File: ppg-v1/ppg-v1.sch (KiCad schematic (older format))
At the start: 67 parts

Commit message: Added everything together, moved things around, added a battery, and made some changes to the circuitry controlling charging etc
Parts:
- removed C?: 1uF, symbol Device:C_Small
- removed D? (x2): IN-S85TATRGB_ALT, rcpaperplane:IN-S85TATRGB, symbol rcpaperplane:IN-S85TATRGB_ALT
- removed R?: 100K, Resistor_SMD:R_0603_1608Metric, symbol Device:R
- removed R?: 1K, Resistor_SMD:R_0603_1608Metric, symbol Device:R
- removed U? (x2): SN74LVC1GU04, Package_TO_SOT_SMD:SOT-353_SC-70-5, symbol rcpaperplane:SN74LVC1GU04
- added BT?: Battery, symbol Device:Battery
- gave numbers to parts that had none: 1
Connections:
- net labels added: VBAT
- wire segments 127 -> 117
- no-connect marks 21 -> 20
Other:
- moved on the sheet: C?, D?, D?A, R?, SW?, U?, U?A, U?B, U?C, UC, Y?

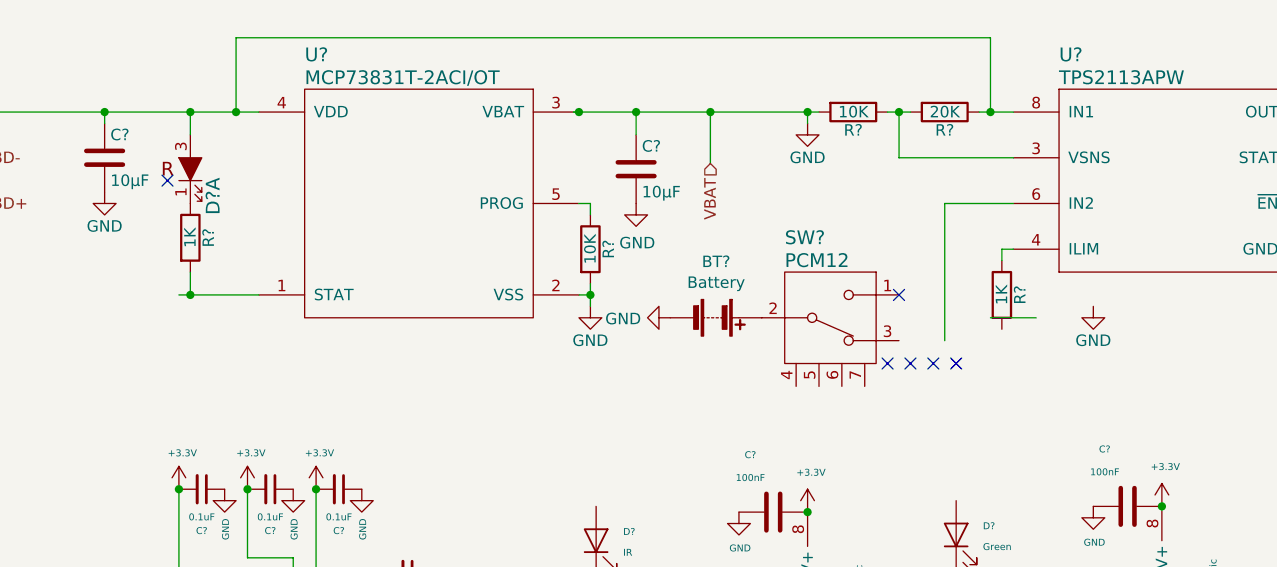
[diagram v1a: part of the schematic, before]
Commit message: Fixed some offset parts and a disconnect between a part and GND
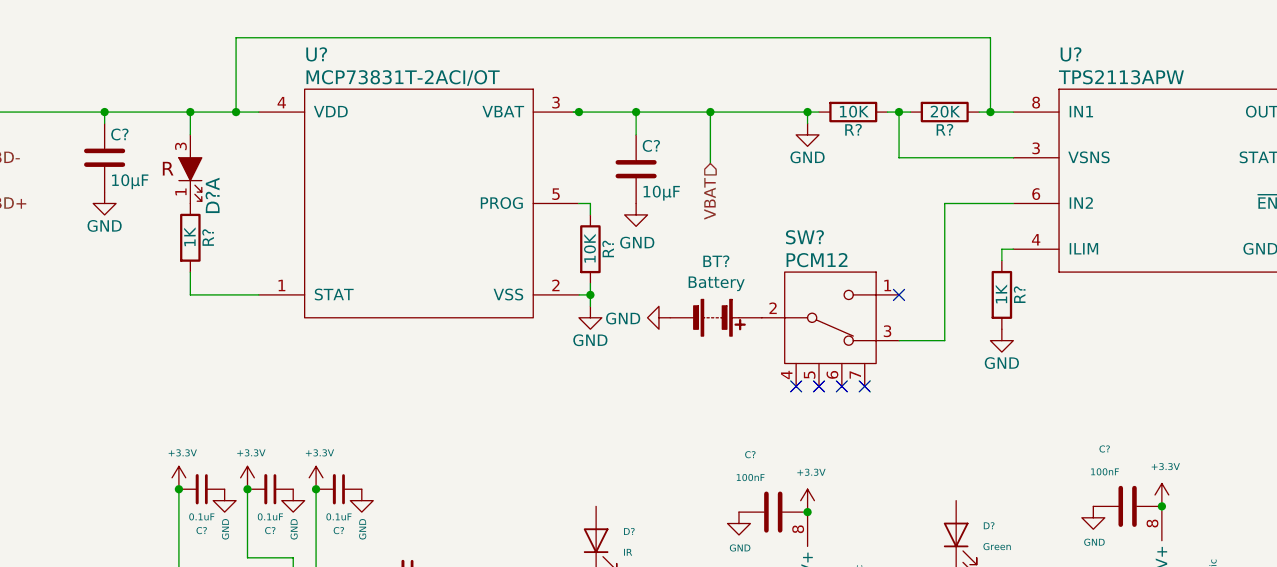
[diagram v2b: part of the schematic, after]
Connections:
- wire segments 117 -> 116
- no-connect marks 20 -> 19
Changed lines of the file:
@@
 Wire Wire Line
 	2375 925  2375 975
-NoConn ~ 2650 1225
 $Comp
 L Device:R R?
@@
 $EndComp
 Wire Wire Line
-	2700 1725 2750 1725
-Wire Wire Line
 	2750 1725 2750 1625
 Wire Wire Line
@@
 L power:GND #PWR0127
 U 1 1 5B12E1D7
-P 6700 1775
-F 0 "#PWR0127" H 6700 1525 50  0001 C CNN
-F 1 "GND" H 6700 1625 50  0000 C CNN
-F 2 "" H 6700 1775 50  0001 C CNN
-F 3 "" H 6700 1775 50  0001 C CNN
-	1    6700 1775
+P 6300 1875
+F 0 "#PWR0127" H 6300 1625 50  0001 C CNN
+F 1 "GND" H 6300 1725 50  0000 C CNN
+F 2 "" H 6300 1875 50  0001 C CNN
+F 3 "" H 6300 1875 50  0001 C CNN
+	1    6300 1875
 	1    0    0    -1
 $EndComp
@@
 	6050 1325 6050 1925
 NoConn ~ 5850 1725
-NoConn ~ 5800 2025
-NoConn ~ 5900 2025
-NoConn ~ 6000 2025
-NoConn ~ 6100 2025
+NoConn ~ 5500 2125
+NoConn ~ 5600 2125
+NoConn ~ 5700 2125
 $Comp
 L Device:C C?
@@
 RX_IND
 Wire Wire Line
-	6450 1825 6250 1825
-Wire Wire Line
 	5850 925  5900 925
 Wire Wire Line
@@
 	0    1    1    0
 $EndComp
-Connection ~ 2750 1725
 Wire Wire Line
 	2750 925  2375 925
 Connection ~ 2750 925
 Connection ~ 2375 925
+NoConn ~ 5400 2125
+Wire Wire Line
+	5850 1925 6050 1925
 $EndSCHEMATC

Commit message: adding everything
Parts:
- removed C? (x2): 8pF, symbol Device:C_Small
- removed C? (x4): 0.1uF, symbol Device:C_Small
- removed Y?: 12M, symbol Device:Crystal_GND24_Small
- added C5, C6, C7, C8: 0.1uF, Capacitor_SMD:C_0603_1608Metric, symbol Device:C_Small
- added J2: Conn_01x04_Male, Connector_PinHeader_2.54mm:PinHeader_1x04_P2.54mm_Vertical, symbol Connector:Conn_01x04_Male
- added Y1: 12MHz, mp3b:CSTNE, symbol Device:Resonator_Small
- BT1: renamed from BT?; footprint (none) -> Connector_PinHeader_2.54mm:PinHeader_1x02_P2.54mm_Vertical
- C1, C10, C11, C12, C13, C2, C4: renamed from C?; footprint (none) -> Capacitor_SMD:C_0603_1608Metric
- D1: renamed from D?; footprint (none) -> LED_SMD:LED_0805_2012Metric
- D3, D6: renamed from D?; footprint (none) -> Connector_PinHeader_2.54mm:PinHeader_1x02_P2.54mm_Vertical
- D4: renamed from D?; value IR -> IR PhotoDiode; footprint (none) -> Connector_PinHeader_2.54mm:PinHeader_1x02_P2.54mm_Vertical
- D5: renamed from D?; value Green -> GreenPhotoDiode; footprint (none) -> Connector_PinHeader_2.54mm:PinHeader_1x02_P2.54mm_Vertical
- R1, R11, R12, R14, R16, R17, R2, R3, R4, R7, R8, R9: renamed from R?; footprint (none) -> Resistor_SMD:R_0603_1608Metric
- SW1, SW2: renamed from SW?; footprint (none) -> Button_Switch_SMD:SW_SPST_B3U-1000P
- U3, U4: renamed from U?; footprint (none) -> ppg-v1:DualOpAmp
- U4: renamed from U; footprint (none) -> ppg-v1:DualOpAmp
- Y2: renamed from Y?; footprint (none) -> ppg-v1:32K28
- gave numbers to parts that had none: 20
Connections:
- net labels added: GreenLED, IRLED, PhotoDiode1, PhotoDiode2
- wire segments 116 -> 118
- no-connect marks 19 -> 45
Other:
- moved on the sheet: C1, C10, C11, C16, C2, C4, D4, D5, D7, R1, R11, R12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

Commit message: Replace led footprint, move switch, route things
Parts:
- removed D2: IN-S85TATRGB_ALT, rcpaperplane:IN-S85TATRGB, symbol rcpaperplane:IN-S85TATRGB_ALT
- added D2: LED_Small, LED_SMD:LED_0805_2012Metric, symbol Device:LED_Small
- J1: symbol rcpaperplane:USB_microB_2040002-1 -> ppg-v1-rescue:USB_microB_2040002-1-rcpaperplane
- SW3: symbol rcpaperplane:PCM12 -> ppg-v1-rescue:PCM12-rcpaperplane
- U2: symbol rcpaperplane1-rescue:MCP73831T-2ACI_OT -> ppg-v1-rescue:MCP73831T-2ACI_OT-rcpaperplane1-rescue
- U5: symbol rcpaperplane:TPS2113APW -> ppg-v1-rescue:TPS2113APW-rcpaperplane
- U6: symbol rcpaperplane1-rescue:MCP1702T-3302E_CB -> ppg-v1-rescue:MCP1702T-3302E_CB-rcpaperplane1-rescue
- U7: symbol rcpaperplane:BM71BLES1FC2 -> ppg-v1-rescue:BM71BLES1FC2-rcpaperplane
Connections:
- net at C3.1, J1.1 (VBUS), R13.1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: now also D2.2 (A)
- net at R5.1: now also D2.1 (K)
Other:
- moved on the sheet: R5
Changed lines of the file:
@@
 EESchema Schematic File Version 4
 LIBS:ppg-v1-cache
-EELAYER 26 0
+EELAYER 29 0
 EELAYER END
 $Descr A4 11693 8268
@@
 $EndComp
 $Comp
-L rcpaperplane:BM71BLES1FC2 U7
+L ppg-v1-rescue:BM71BLES1FC2-rcpaperplane U7
 U 1 1 5B12B5AE
 P 8570 3065
@@
 $EndComp
 $Comp
-L rcpaperplane:PCM12 SW3
+L ppg-v1-rescue:PCM12-rcpaperplane SW3
 U 1 1 5B12B697
 P 5550 1825
@@
 $EndComp
 $Comp
-L rcpaperplane:USB_microB_2040002-1 J1
+L ppg-v1-rescue:USB_microB_2040002-1-rcpaperplane J1
 U 1 1 5B12B6CA
 P 1075 1325
@@
 $EndComp
 $Comp
-L rcpaperplane:TPS2113APW U5
+L ppg-v1-rescue:TPS2113APW-rcpaperplane U5
 U 1 1 5B12B707
 P 7050 1225
@@
 F 3 "" H 7050 1225 60  0001 C CNN
 	1    7050 1225
-	1    0    0    -1
-$EndComp
-$Comp
-L rcpaperplane:IN-S85TATRGB_ALT D2
-U 1 1 5B12BF1D
-P 2750 1175
-F 0 "D2" V 2850 975 60  0000 L CNN
-F 1 "IN-S85TATRGB_ALT" V 2950 975 60  0001 L CNN
-F 2 "rcpaperplane:IN-S85TATRGB" H 2750 1175 60  0001 C CNN
-F 3 "" H 2750 1175 60  0001 C CNN
-	1    2750 1175
 	1    0    0    -1
 $EndComp
@@
 L Device:R R5
 U 1 1 5B12D828
-P 2750 1475
-F 0 "R5" V 2830 1475 50  0000 C CNN
-F 1 "1K" V 2750 1475 50  0000 C CNN
-F 2 "Resistor_SMD:R_0603_1608Metric" V 2680 1475 50  0001 C CNN
-F 3 "" H 2750 1475 50  0001 C CNN
-	1    2750 1475
-	1    0    0    -1
-$EndComp
-Wire Wire Line
-	2750 1725 2750 1625
+P 2750 1375
+F 0 "R5" V 2830 1375 50  0000 C CNN
+F 1 "1K" V 2750 1375 50  0000 C CNN
+F 2 "Resistor_SMD:R_0603_1608Metric" V 2680 1375 50  0001 C CNN
+F 3 "" H 2750 1375 50  0001 C CNN
+	1    2750 1375
+	1    0    0    -1
+$EndComp
+Wire Wire Line
+	2750 1725 2750 1525
 Wire Wire Line
 	2750 1025 2750 925
@@
 Connection ~ 9550 925
 $Comp
-L rcpaperplane1-rescue:MCP1702T-3302E_CB U6
+L ppg-v1-rescue:MCP1702T-3302E_CB-rcpaperplane1-rescue U6
 U 1 1 5B12B607
 P 8850 925
@@
 	4425 925  4450 925
 $Comp
-L rcpaperplane1-rescue:MCP73831T-2ACI_OT U2
+L ppg-v1-rescue:MCP73831T-2ACI_OT-rcpaperplane1-rescue U2
 U 1 1 5B12B660
 P 3750 1325
@@
 	1    0    0    -1
 $EndComp
+$Comp
+L Device:LED_Small D2
+U 1 1 5CB87F94
+P 2750 1125
+F 0 "D2" H 2750 1230 30  0000 C CNN
+F 1 "LED_Small" H 2760 1060 30  0000 C CNN
+F 2 "LED_SMD:LED_0805_2012Metric" V 2750 1125 30  0001 C CNN
+F 3 "~" V 2750 1125 30  0001 C CNN
+	1    2750 1125
+	0    -1   -1   0
+$EndComp
 $EndSCHEMATC

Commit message: Rebuilding pcb layout
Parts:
- J1: symbol ppg-v1-rescue:USB_microB_2040002-1-rcpaperplane -> ppg-v1-rescue:USB_microB_2040002-1-rcpaperplane-ppg-v1-rescue
- SW3: symbol ppg-v1-rescue:PCM12-rcpaperplane -> ppg-v1-rescue:PCM12-rcpaperplane-ppg-v1-rescue
- U2: symbol ppg-v1-rescue:MCP73831T-2ACI_OT-rcpaperplane1-rescue -> ppg-v1-rescue:MCP73831T-2ACI_OT-rcpaperplane1-rescue-ppg-v1-rescue
- U5: symbol ppg-v1-rescue:TPS2113APW-rcpaperplane -> ppg-v1-rescue:TPS2113APW-rcpaperplane-ppg-v1-rescue
- U6: symbol ppg-v1-rescue:MCP1702T-3302E_CB-rcpaperplane1-rescue -> ppg-v1-rescue:MCP1702T-3302E_CB-rcpaperplane1-rescue-ppg-v1-rescue
- U7: symbol ppg-v1-rescue:BM71BLES1FC2-rcpaperplane -> ppg-v1-rescue:BM71BLES1FC2-rcpaperplane-ppg-v1-rescue
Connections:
- wire segments 118 -> 154
- no-connect marks 45 -> 33
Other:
- moved on the sheet: J2, U3B, U4A
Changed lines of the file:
@@
 EESchema Schematic File Version 4
 LIBS:ppg-v1-cache
-EELAYER 29 0
+EELAYER 26 0
 EELAYER END
 $Descr A4 11693 8268
@@
 $EndComp
 $Comp
-L ppg-v1-rescue:BM71BLES1FC2-rcpaperplane U7
-U 1 1 5B12B5AE
-P 8570 3065
-F 0 "U7" H 7770 4115 60  0000 L CNN
-F 1 "BM71BLES1FC2" H 7770 4015 30  0000 L CNN
-F 2 "rcpaperplane:BM71BLES1FC2" H 8820 2815 60  0001 C CNN
-F 3 "" H 8820 2815 60  0001 C CNN
-	1    8570 3065
-	1    0    0    -1
-$EndComp
-$Comp
-L ppg-v1-rescue:PCM12-rcpaperplane SW3
+L ppg-v1-rescue:PCM12-rcpaperplane-ppg-v1-rescue SW3
 U 1 1 5B12B697
 P 5550 1825
@@
 $EndComp
 $Comp
-L ppg-v1-rescue:USB_microB_2040002-1-rcpaperplane J1
+L ppg-v1-rescue:USB_microB_2040002-1-rcpaperplane-ppg-v1-rescue J1
 U 1 1 5B12B6CA
 P 1075 1325
@@
 $EndComp
 $Comp
-L ppg-v1-rescue:TPS2113APW-rcpaperplane U5
+L ppg-v1-rescue:TPS2113APW-rcpaperplane-ppg-v1-rescue U5
 U 1 1 5B12B707
 P 7050 1225
@@
 L power:GND #PWR052
 U 1 1 5B13111F
-P 9865 2860
-F 0 "#PWR052" H 9865 2610 50  0001 C CNN
-F 1 "GND" H 9865 2710 30  0000 C CNN
-F 2 "" H 9865 2860 50  0001 C CNN
-F 3 "" H 9865 2860 50  0001 C CNN
-	1    9865 2860
+P 9865 2840
+F 0 "#PWR052" H 9865 2590 50  0001 C CNN
+F 1 "GND" H 9865 2690 30  0000 C CNN
+F 2 "" H 9865 2840 50  0001 C CNN
+F 3 "" H 9865 2840 50  0001 C CNN
+	1    9865 2840
 	-1   0    0    1
 $EndComp
@@
 Connection ~ 9550 925
 $Comp
-L ppg-v1-rescue:MCP1702T-3302E_CB-rcpaperplane1-rescue U6
+L ppg-v1-rescue:MCP1702T-3302E_CB-rcpaperplane1-rescue-ppg-v1-rescue U6
 U 1 1 5B12B607
 P 8850 925
@@
 L Device:Opamp_Dual_Generic U4
 U 1 1 5CAF65B0
-P 6450 4525
-F 0 "U4" H 6600 4650 30  0000 C CNN
-F 1 "Opamp_Dual_Generic" H 6750 4725 30  0000 C CNN
-F 2 "ppg-v1:DualOpAmp" H 6450 4525 50  0001 C CNN
-F 3 "~" H 6450 4525 50  0001 C CNN
-	1    6450 4525
+P 5225 5950
+F 0 "U4" H 5375 6075 30  0000 C CNN
+F 1 "Opamp_Dual_Generic" H 5525 6150 30  0000 C CNN
+F 2 "ppg-v1:DualOpAmp" H 5225 5950 50  0001 C CNN
+F 3 "~" H 5225 5950 50  0001 C CNN
+	1    5225 5950
 	1    0    0    1
 $EndComp
@@
 Wire Wire Line
 	6150 4125 6300 4125
-Connection ~ 6150 4425
 Wire Wire Line
 	6600 4125 6750 4125
@@
 L Device:Opamp_Dual_Generic U3
 U 2 1 5CB2F6C0
-P 5225 5950
-F 0 "U3" H 5400 6075 30  0000 C CNN
-F 1 "Opamp_Dual_Generic" H 5475 6175 30  0000 C CNN
-F 2 "ppg-v1:DualOpAmp" H 5225 5950 50  0001 C CNN
-F 3 "~" H 5225 5950 50  0001 C CNN
-	2    5225 5950
+P 6450 4525
+F 0 "U3" H 6625 4650 30  0000 C CNN
+F 1 "Opamp_Dual_Generic" H 6700 4750 30  0000 C CNN
+F 2 "ppg-v1:DualOpAmp" H 6450 4525 50  0001 C CNN
+F 3 "~" H 6450 4525 50  0001 C CNN
+	2    6450 4525
 	1    0    0    1
 $EndComp
@@
 	-1   0    0    1
 $EndComp
-Wire Wire Line
-	1725 925  2375 925
 Connection ~ 5450 2675
 Wire Wire Line
 	4425 925  4450 925
 $Comp
-L ppg-v1-rescue:MCP73831T-2ACI_OT-rcpaperplane1-rescue U2
+L ppg-v1-rescue:MCP73831T-2ACI_OT-rcpaperplane1-rescue-ppg-v1-rescue U2
 U 1 1 5B12B660
 P 3750 1325
@@
 	0    1    1    0
 $EndComp
-Wire Wire Line
-	2750 925  2375 925
 Connection ~ 2750 925
-Connection ~ 2375 925
 NoConn ~ 5400 2125
 Wire Wire Line
@@
 NoConn ~ 2500 4575
 NoConn ~ 2500 4675
-NoConn ~ 2500 4875
-NoConn ~ 2500 4975
-NoConn ~ 2500 5075
-NoConn ~ 2500 5275
-NoConn ~ 2500 5375
-NoConn ~ 2500 5175
 NoConn ~ 3800 4475
 NoConn ~ 3800 4675
 NoConn ~ 3800 4875
 NoConn ~ 3800 5075
-NoConn ~ 3800 5275
-NoConn ~ 3800 5375
-NoConn ~ 3800 5475
-NoConn ~ 3800 5775
-NoConn ~ 3800 5875
-NoConn ~ 3800 5975
-Wire Wire Line
-	2500 5975 2250 5975
-Wire Wire Line
-	2500 5875 2250 5875
-Wire Wire Line
-	2500 5775 2250 5775
-Wire Wire Line
-	2500 5675 2250 5675
 Wire Wire Line
 	5350 5300 5525 5300
@@
 Text GLabel 3800 5175 2    30   Input ~ 0
 GreenLED
-NoConn ~ 8070 4065
-NoConn ~ 8270 4065
-NoConn ~ 8470 4065
-NoConn ~ 8670 4065
-NoConn ~ 8870 4065
-NoConn ~ 9070 4065
 Text GLabel 5025 1150 3    30   Input ~ 0
 VBAT
@@
 Wire Wire Line
 	2830 3000 3100 3000
-$Comp
-L MCU_ST_STM32F4:STM32F411CEUx U1
-U 1 1 5CA9479A
-P 3200 4575
-F 0 "U1" H 3225 5150 30  0000 C CNN
-F 1 "STM32F411CEUx" H 3250 5025 30  0000 C CNN
-F 2 "Package_DFN_QFN:QFN-48-1EP_7x7mm_P0.5mm_EP5.6x5.6mm" H 2600 3075 30  0001 R CNN
-F 3 "http://www.st.com/st-web-ui/static/active/en/resource/technical/document/datasheet/DM00115249.pdf" H 3200 4575 30  0001 C CNN
-	1    3200 4575
-	1    0    0    -1
-$EndComp
 Wire Wire Line
 	2450 4175 2500 4175
@@
 	4925 5300 4925 5610
 Wire Wire Line
-	5525 5610 5525 5950
-Wire Wire Line
 	4925 5610 4925 5850
 Connection ~ 5500 4215
@@
 	5500 4625 5500 4525
 Connection ~ 5500 4525
-Connection ~ 4925 5850
-Connection ~ 5525 5950
-Wire Wire Line
-	5525 5950 5525 6050
 NoConn ~ 2500 5475
 NoConn ~ 2500 5575
@@
 L Connector:Conn_01x04_Male J2
 U 1 1 5D0E1BBA
-P 2050 5775
-F 0 "J2" H 2156 6053 50  0000 C CNN
-F 1 "Conn_01x04_Male" H 2156 5962 50  0000 C CNN
-F 2 "Connector_PinHeader_2.54mm:PinHeader_1x04_P2.54mm_Vertical" H 2050 5775 50  0001 C CNN
-F 3 "~" H 2050 5775 50  0001 C CNN
-	1    2050 5775
+P 1610 6075
+F 0 "J2" H 1716 6353 50  0000 C CNN
+F 1 "Conn_01x04_Male" H 1716 6262 50  0000 C CNN
+F 2 "Connector_PinHeader_2.54mm:PinHeader_1x04_P2.54mm_Vertical" H 1610 6075 50  0001 C CNN
+F 3 "~" H 1610 6075 50  0001 C CNN
+	1    1610 6075
 	1    0    0    -1
 $EndComp
@@
 	0    -1   -1   0
 $EndComp
+Connection ~ 6150 4425
+Wire Wire Line
+	3800 5875 3925 5875
+Wire Wire Line
+	3925 5875 3925 6425
+NoConn ~ 2500 4975
+NoConn ~ 2500 5175
+NoConn ~ 2500 5375
+NoConn ~ 3800 5775
+$Comp
+L ppg-v1-rescue:BM71BLES1FC2-rcpaperplane-ppg-v1-rescue U7
+U 1 1 5B12B5AE
+P 8570 3065
+F 0 "U7" H 7770 4115 60  0000 L CNN
+F 1 "BM71BLES1FC2" H 7770 4015 30  0000 L CNN
+F 2 "rcpaperplane:BM71BLES1FC2" H 8820 2815 60  0001 C CNN
+F 3 "" H 8820 2815 60  0001 C CNN
+	1    8570 3065
+	1    0    0    -1
+$EndComp
+Text Label 2385 5675 2    60   ~ 0
+CTS
+Text Label 2445 5775 2    60   ~ 0
+RST_N
+Text Label 2480 5875 2    60   ~ 0
+RTS
+Text Label 2460 5975 2    60   ~ 0
+TX
+Text Label 3885 5275 0    60   ~ 0
+RX
+Wire Wire Line
+	1930 5075 2500 5075
+Wire Wire Line
+	1855 4875 2500 4875
+Wire Wire Line
+	1855 6075 1810 6075
+Wire Wire Line
+	1855 4875 1855 6075
+Wire Wire Line
+	1930 5075 1930 6175
+Wire Wire Line
+	1810 6175 1930 6175
+Wire Wire Line
+	1805 6275 1810 6275
+Connection ~ 1810 6275
+Wire Wire Line
+	1810 6275 2000 6275
+Wire Wire Line
+	3925 6425 1810 6425
+Wire Wire Line
+	1810 6425 1810 6380
+$Comp
+L MCU_ST_STM32F4:STM32F411CEUx U1
+U 1 1 5CA9479A
+P 3200 4575
+F 0 "U1" H 3225 5150 30  0000 C CNN
+F 1 "STM32F411CEUx" H 3250 5025 30  0000 C CNN
+F 2 "Package_DFN_QFN:QFN-48-1EP_7x7mm_P0.5mm_EP5.6x5.6mm" H 2600 3075 30  0001 R CNN
+F 3 "http://www.st.com/st-web-ui/static/active/en/resource/technical/document/datasheet/DM00115249.pdf" H 3200 4575 30  0001 C CNN
+	1    3200 4575
+	1    0    0    -1
+$EndComp
+Wire Wire Line
+	3795 5375 3795 5380
+Connection ~ 5525 5950
+Connection ~ 4925 5850
+Wire Wire Line
+	5525 5950 5525 6050
+Wire Wire Line
+	5525 5610 5525 5950
+Wire Wire Line
+	2500 5275 2000 5275
+Wire Wire Line
+	2000 5270 2000 5275
+Connection ~ 2000 5275
+Wire Wire Line
+	2000 5275 2000 6275
+Text Label 3915 5375 0    60   ~ 0
+RX_IND
+Wire Wire Line
+	2480 5875 2500 5875
+Wire Wire Line
+	3800 5275 3885 5275
+NoConn ~ 3800 5475
+Wire Wire Line
+	1725 925  2375 925
+Connection ~ 2375 925
+Wire Wire Line
+	2375 925  2750 925
+Connection ~ 2500 5975
+Wire Wire Line
+	2500 5975 2510 5975
+Wire Wire Line
+	2460 5975 2500 5975
+Connection ~ 2500 5775
+Wire Wire Line
+	2500 5775 2505 5775
+Wire Wire Line
+	2445 5775 2500 5775
+Connection ~ 2500 5675
+Wire Wire Line
+	2500 5675 2505 5675
+Wire Wire Line
+	2385 5675 2500 5675
+Wire Wire Line
+	3800 5375 3915 5375
+Wire Wire Line
+	3800 5375 3795 5375
+Connection ~ 3800 5375
+NoConn ~ 3800 5975
+Wire Wire Line
+	9865 2865 9865 2840
+Wire Wire Line
+	1810 6380 2165 6380
+Wire Wire Line
+	2165 6380 2165 5980
+Wire Wire Line
+	2165 5980 2080 5980
+Wire Wire Line
+	2080 5980 2080 6035
+Wire Wire Line
+	2080 6035 2130 6035
+Wire Wire Line
+	2130 6035 2130 5920
+Wire Wire Line
+	2130 5920 2065 5920
+Wire Wire Line
+	2065 5920 2065 5960
+Wire Wire Line
+	2065 5960 2090 5960
+Wire Wire Line
+	2090 5960 2090 5875
+Wire Wire Line
+	2090 5875 1810 5875
+Wire Wire Line
+	1810 5875 1810 5975
+Connection ~ 1810 6380
+Wire Wire Line
+	1810 6380 1810 6375
 $EndSCHEMATC
